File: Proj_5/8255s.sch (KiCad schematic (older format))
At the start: 3 parts

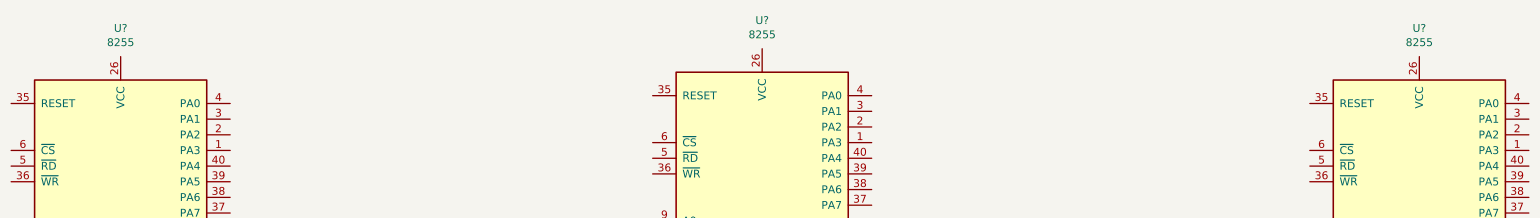
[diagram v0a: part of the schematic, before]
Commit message: Added address decoding
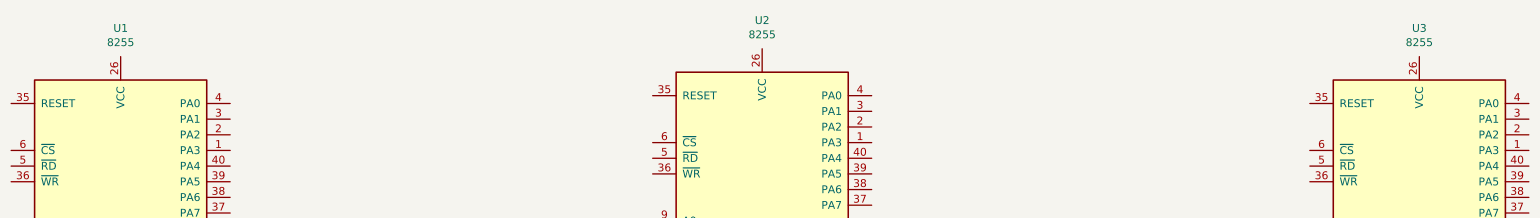
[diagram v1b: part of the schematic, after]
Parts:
- gave numbers to parts that had none: 3
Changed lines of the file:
@@
 $EndDescr
 $Comp
-L Interface:8255 U?
+L Interface:8255 U1
 U 1 1 5E9F9AC1
 P 4450 5450
-F 0 "U?" H 4450 7231 50  0000 C CNN
+F 0 "U1" H 4450 7231 50  0000 C CNN
 F 1 "8255" H 4450 7140 50  0000 C CNN
 F 2 "Package_DIP:DIP-40_W15.24mm" H 4450 5750 50  0001 C CNN
@@
 $EndComp
 $Comp
-L Interface:8255 U?
+L Interface:8255 U2
 U 1 1 5E9FFD77
 P 8550 5400
-F 0 "U?" H 8550 7181 50  0000 C CNN
+F 0 "U2" H 8550 7181 50  0000 C CNN
 F 1 "8255" H 8550 7090 50  0000 C CNN
 F 2 "Package_DIP:DIP-40_W15.24mm" H 8550 5700 50  0001 C CNN
@@
 $EndComp
 $Comp
-L Interface:8255 U?
+L Interface:8255 U3
 U 1 1 5EA0128E
 P 12750 5450
-F 0 "U?" H 12750 7231 50  0000 C CNN
+F 0 "U3" H 12750 7231 50  0000 C CNN
 F 1 "8255" H 12750 7140 50  0000 C CNN
 F 2 "Package_DIP:DIP-40_W15.24mm" H 12750 5750 50  0001 C CNN

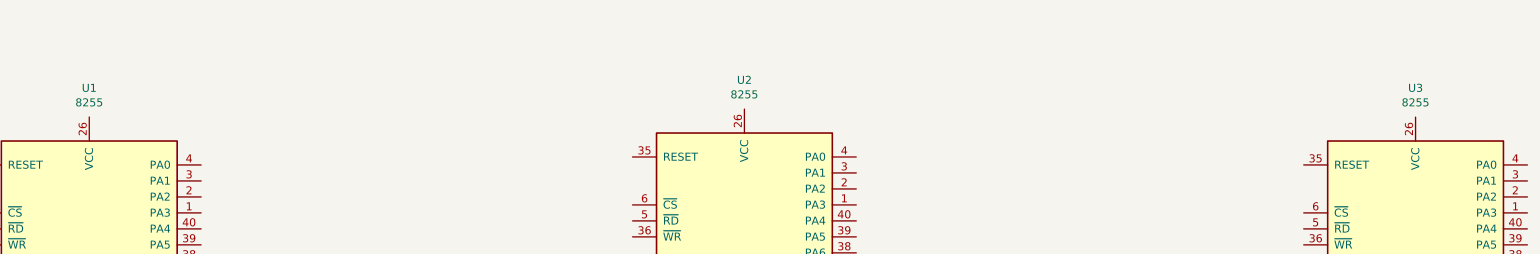
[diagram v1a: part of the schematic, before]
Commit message: Added Caps to Each Vcc per desc.
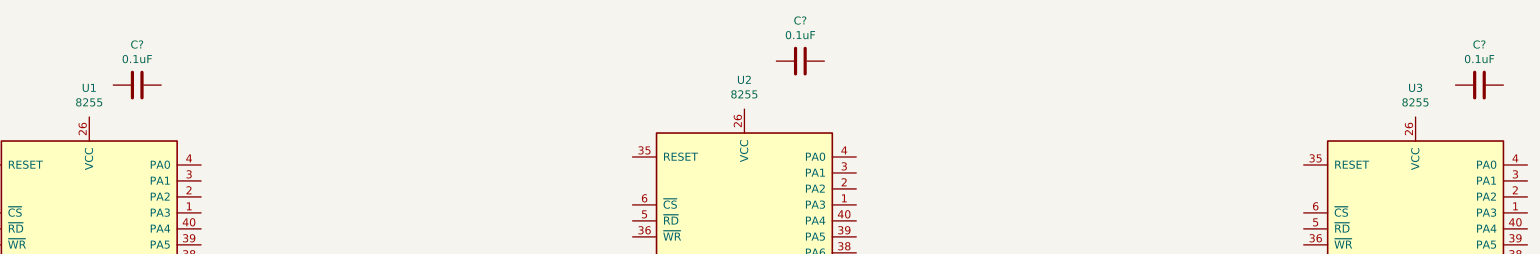
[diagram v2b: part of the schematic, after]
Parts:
- added C? (x3): 0.1uF, symbol Device:C
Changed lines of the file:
@@
 $Descr A3 16535 11693
 encoding utf-8
-Sheet 4 11
+Sheet 3 11
 Title ""
 Date ""
@@
 	1    0    0    -1
 $EndComp
+$Comp
+L Device:C C?
+U 1 1 5EA6A7B2
+P 4750 3650
+F 0 "C?" V 4498 3650 50  0000 C CNN
+F 1 "0.1uF" V 4589 3650 50  0000 C CNN
+F 2 "" H 4788 3500 50  0001 C CNN
+F 3 "~" H 4750 3650 50  0001 C CNN
+	1    4750 3650
+	0    1    1    0
+$EndComp
+$Comp
+L Device:C C?
+U 1 1 5EA6AA16
+P 8900 3500
+F 0 "C?" V 8648 3500 50  0000 C CNN
+F 1 "0.1uF" V 8739 3500 50  0000 C CNN
+F 2 "" H 8938 3350 50  0001 C CNN
+F 3 "~" H 8900 3500 50  0001 C CNN
+	1    8900 3500
+	0    1    1    0
+$EndComp
+$Comp
+L Device:C C?
+U 1 1 5EA6B47A
+P 13150 3650
+F 0 "C?" V 12898 3650 50  0000 C CNN
+F 1 "0.1uF" V 12989 3650 50  0000 C CNN
+F 2 "" H 13188 3500 50  0001 C CNN
+F 3 "~" H 13150 3650 50  0001 C CNN
+	1    13150 3650
+	0    1    1    0
+$EndComp
 $EndSCHEMATC
